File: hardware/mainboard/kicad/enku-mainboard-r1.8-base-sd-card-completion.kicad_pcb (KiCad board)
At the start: 4 copper layers, 59 x 101 mm, 132 parts, among them J1 1S LiPo + NTC, J2 Hirose DM3AT-SF-PEJM5, J3 FH34SRJ-24S-0.5SH(50), J5 GCT USB4105-GF-A-120, J6 4-pin pogo dock, J7 Tag-Connect TC2030-IDC-NL, Q1 IRLML6346TRPBF, Q2 AO3401A, SW1 HARD POWER, SW2 BOOT / RECOVERY, SW3 BTN_L1, SW4 BTN_L2, SW5 BTN_R1, SW6 BTN_R2, U1 ESP32-S3-WROOM-1-N16R8, U10 TLV3012BIDBVR, U2 TPS2121, U3 BQ25185DLHR, U4 TPS63802DLAR, U5 BMI270, U8 USBLC6-2SC6, U9 TMUX1101DBVR

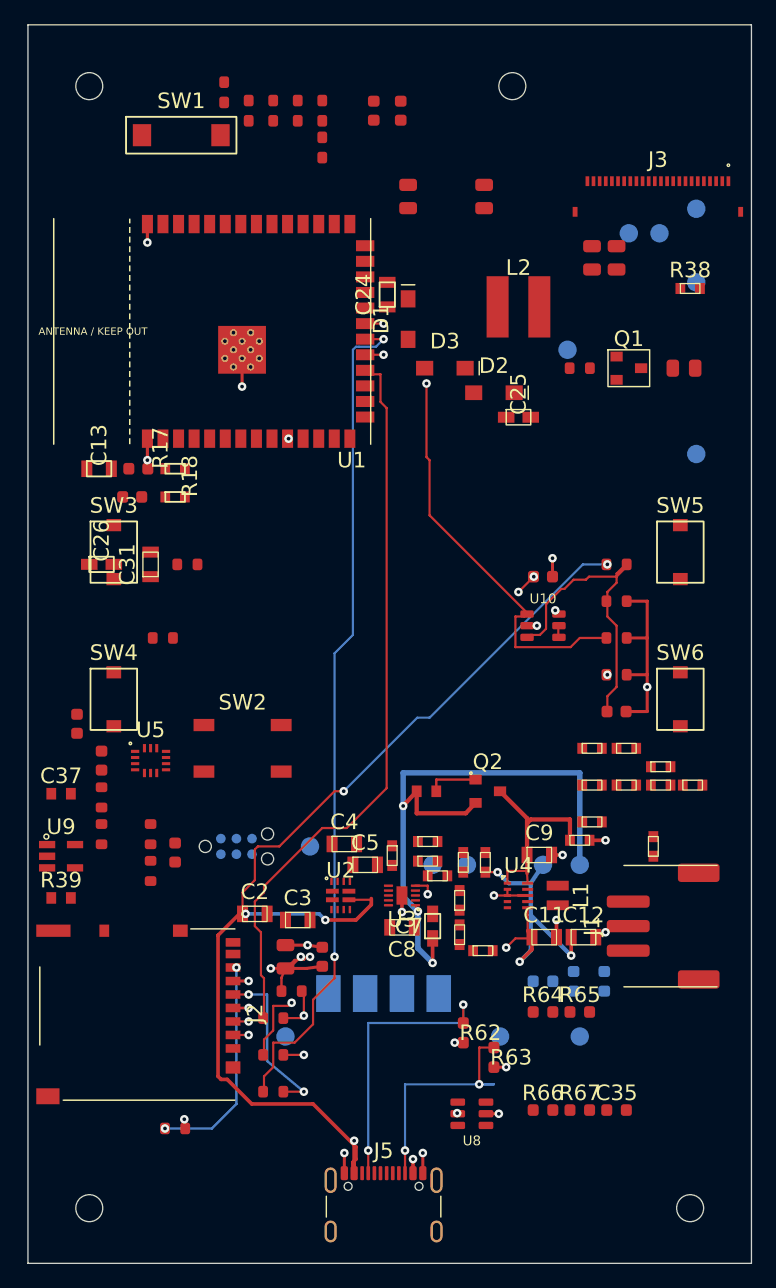
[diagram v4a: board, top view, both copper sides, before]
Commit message: R41: move new plated via holes out of SD, comparator and USB SMD lands
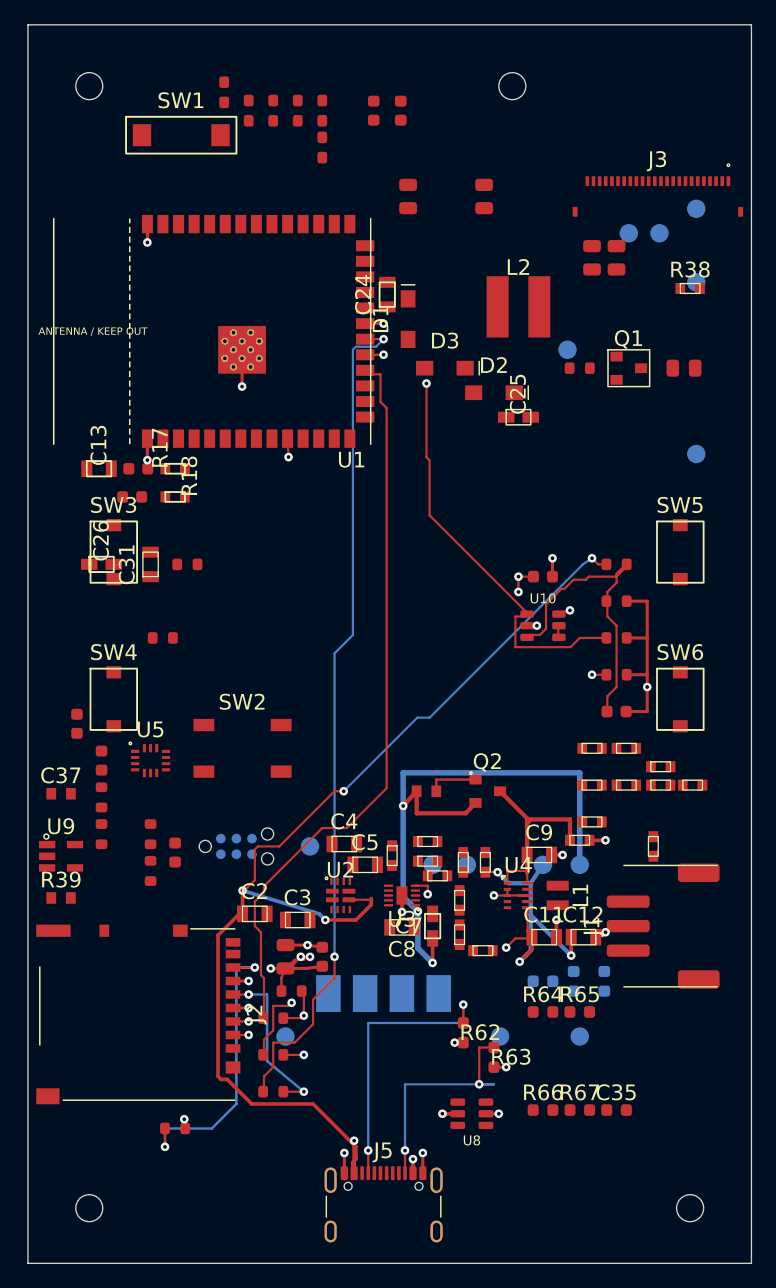
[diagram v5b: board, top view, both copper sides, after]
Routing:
- net VBUS_USB: track 134.1 -> 140.3 mm
- net SD_MISO_CARD: track 18.1 -> 24.1 mm
- net USB_VBUS_VALID: track 54.8 -> 57.8 mm
- net 3V3_SYS: track 101.8 -> 104.7 mm
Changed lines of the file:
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@@
   (segment (start 40.5 100.8) (end 40.3 101) (width 0.18) (layer "F.Cu") (net 9))
   (segment (start 40.3 101) (end 38.825 101) (width 0.18) (layer "F.Cu") (net 9))
-  (segment (start 34.725 96.875) (end 35 96.875) (width 0.18) (layer "F.Cu") (net 12))
+  (segment (start 34.725 96.875) (end 36.5 96.875) (width 0.18) (layer "F.Cu") (net 12))
   (segment (start 35 96.875) (end 35 108) (width 0.2) (layer "B.Cu") (net 12))
   (segment (start 35 108) (end 33 110) (width 0.2) (layer "B.Cu") (net 12))
@@
   (via (at 36 102.375) (size 0.70) (drill 0.30) (layers "F.Cu" "B.Cu") (net 9))
   (via (at 40.5 100.8) (size 0.70) (drill 0.30) (layers "F.Cu" "B.Cu") (net 9))
-  (via (at 35 96.875) (size 0.70) (drill 0.30) (layers "F.Cu" "B.Cu") (net 12))
-  (via (at 29.175 110) (size 0.70) (drill 0.30) (layers "F.Cu" "B.Cu") (net 12))
+  (via (at 36.5 96.875) (size 0.70) (drill 0.30) (layers "F.Cu" "B.Cu") (net 12))
+  (via (at 29.175 111.5) (size 0.70) (drill 0.30) (layers "F.Cu" "B.Cu") (net 12))
   (segment (start 45.5 48.25) (end 45.75 48.5) (width 0.18) (layer "F.Cu") (net 60))
   (segment (start 45.75 48.5) (end 46.75 48.5) (width 0.18) (layer "F.Cu") (net 60))
@@
   (segment (start 47.5 43.5) (end 46.5 43.5) (width 0.18) (layer "In1.Cu") (net 97))
   (segment (start 46.5 43.5) (end 39.25 50.75) (width 0.18) (layer "In1.Cu") (net 97))
-  (segment (start 39.25 50.75) (end 39.25 53.75) (width 0.18) (layer "In1.Cu") (net 97))
+  (segment (start 39.25 50.75) (end 39.25 55.25) (width 0.18) (layer "In1.Cu") (net 97))
   (via (at 50.5 49.25) (size 0.70) (drill 0.30) (layers "F.Cu" "B.Cu") (net 97))
-  (via (at 39.25 53.75) (size 0.70) (drill 0.30) (layers "F.Cu" "B.Cu") (net 97))
-  (segment (start 61.25 68.0) (end 61.0 67.75) (width 0.18) (layer "F.Cu") (net 2))
-  (segment (start 61.0 67.75) (end 59.25 66.0) (width 0.18) (layer "In1.Cu") (net 2))
-  (segment (start 59.25 66.0) (end 59.25 65.0) (width 0.18) (layer "In1.Cu") (net 2))
-  (via (at 61.0 67.75) (size 0.70) (drill 0.30) (layers "F.Cu" "B.Cu") (net 2))
-  (via (at 59.25 65.0) (size 0.70) (drill 0.30) (layers "F.Cu" "B.Cu") (net 2))
-  (segment (start 59.25 65.0) (end 58.0 66.25) (width 0.18) (layer "F.Cu") (net 2))
+  (via (at 39.25 55.25) (size 0.70) (drill 0.30) (layers "F.Cu" "B.Cu") (net 97))
+  (segment (start 61.25 68.0) (end 62.2 67.75) (width 0.18) (layer "F.Cu") (net 2))
+  (segment (start 62.2 67.75) (end 59.25 66.0) (width 0.18) (layer "In1.Cu") (net 2))
+  (segment (start 59.25 66.0) (end 58 65) (width 0.18) (layer "In1.Cu") (net 2))
+  (via (at 62.2 67.75) (size 0.70) (drill 0.30) (layers "F.Cu" "B.Cu") (net 2))
+  (via (at 58 65) (size 0.70) (drill 0.30) (layers "F.Cu" "B.Cu") (net 2))
+  (segment (start 58 65) (end 58.0 66.25) (width 0.18) (layer "F.Cu") (net 2))
   (segment (start 58.0 66.25) (end 49.5 74.75) (width 0.18) (layer "In1.Cu") (net 2))
   (segment (start 49.5 74.75) (end 49.5 84.25) (width 0.18) (layer "In1.Cu") (net 2))
@@
   (segment (start 49.75 76.5) (end 50.75 76.5) (width 0.18) (layer "B.Cu") (net 3))
   (segment (start 50.75 76.5) (end 63.25 64.0) (width 0.18) (layer "B.Cu") (net 3))
-  (segment (start 63.25 64.0) (end 65.25 64.0) (width 0.18) (layer "B.Cu") (net 3))
+  (segment (start 63.25 64.0) (end 64 63.5) (width 0.18) (layer "B.Cu") (net 3))
   (via (at 43.75 82.5) (size 0.70) (drill 0.30) (layers "F.Cu" "B.Cu") (net 3))
-  (via (at 65.25 64.0) (size 0.70) (drill 0.30) (layers "F.Cu" "B.Cu") (net 3))
-  (segment (start 65.25 64.0) (end 65.25 73.0) (width 0.18) (layer "In1.Cu") (net 3))
-  (via (at 65.25 73.0) (size 0.70) (drill 0.30) (layers "F.Cu" "B.Cu") (net 3))
+  (via (at 64 63.5) (size 0.70) (drill 0.30) (layers "F.Cu" "B.Cu") (net 3))
+  (segment (start 64 63.5) (end 64 73) (width 0.18) (layer "In1.Cu") (net 3))
+  (via (at 64 73) (size 0.70) (drill 0.30) (layers "F.Cu" "B.Cu") (net 3))
   (zone (net 1) (net_name "GND") (layer "In1.Cu") (hatch edge 0.5)
     (connect_pads (clearance 0.25))
@@
   (segment (start 33.5 94.25) (end 35.25 92.5) (width 0.30) (layer "F.Cu") (net 3))
   (segment (start 35.25 92.5) (end 35.5 92.5) (width 0.30) (layer "F.Cu") (net 3))
-  (segment (start 35.5 92.5) (end 35.75 92.5) (width 0.30) (layer "F.Cu") (net 3))
-  (segment (start 35.75 92.5) (end 41.75 92.5) (width 0.30) (layer "B.Cu") (net 3))
+  (segment (start 35.5 92.5) (end 35.5 90.6) (width 0.30) (layer "F.Cu") (net 3))
+  (segment (start 35.5 90.6) (end 41.75 92.5) (width 0.30) (layer "B.Cu") (net 3))
   (segment (start 41.75 92.5) (end 42.25 93.0) (width 0.30) (layer "B.Cu") (net 3))
   (segment (start 42.25 93.0) (end 44.75 93.0) (width 0.30) (layer "F.Cu") (net 3))
   (segment (start 44.75 93.0) (end 46.0 91.75) (width 0.30) (layer "F.Cu") (net 3))
   (segment (start 46.0 91.75) (end 46.0 91.25) (width 0.30) (layer "F.Cu") (net 3))
-  (via (at 35.75 92.5) (size 0.70) (drill 0.30) (layers "F.Cu" "B.Cu") (net 3))
+  (via (at 35.5 90.6) (size 0.70) (drill 0.30) (layers "F.Cu" "B.Cu") (net 3))
   (via (at 42.25 93.0) (size 0.70) (drill 0.30) (layers "F.Cu" "B.Cu") (net 3))
-  (segment (start 35.5 92.5) (end 35.75 92.5) (width 0.30) (layer "F.Cu") (net 3))
-  (segment (start 35.75 92.5) (end 38.75 95.75) (width 0.30) (layer "In1.Cu") (net 3))
+  (segment (start 35.5 90.6) (end 38.75 95.75) (width 0.30) (layer "In1.Cu") (net 3))
   (segment (start 38.75 95.75) (end 38.75 100.5) (width 0.30) (layer "In1.Cu") (net 3))
   (segment (start 38.75 100.5) (end 45.25 107.0) (width 0.30) (layer "In1.Cu") (net 3))
   (segment (start 45.25 107.0) (end 51.25 107.0) (width 0.30) (layer "In1.Cu") (net 3))
-  (segment (start 51.25 107.0) (end 53.0 108.75) (width 0.30) (layer "In1.Cu") (net 3))
-  (via (at 53.0 108.75) (size 0.70) (drill 0.30) (layers "F.Cu" "B.Cu") (net 3))
+  (segment (start 51.25 107.0) (end 51.8 108.8) (width 0.30) (layer "In1.Cu") (net 3))
+  (via (at 51.8 108.8) (size 0.70) (drill 0.30) (layers "F.Cu" "B.Cu") (net 3))
   (segment (start 54.8 103.4) (end 56 103.4) (width 0.18) (layer "F.Cu") (net 5))
-)
+  (segment (start 36.5 96.875) (end 35 96.875) (width .2) (layer "B.Cu") (net 12))
+  (segment (start 29.175 110) (end 29.175 111.5) (width .2) (layer "B.Cu") (net 12))
+  (segment (start 29.175 110) (end 29.175 111.5) (width .18) (layer "F.Cu") (net 12))
+  (segment (start 39.175 53.75) (end 39.25 55.25) (width .18) (layer "F.Cu") (net 97))
+  (segment (start 58 65) (end 59.225 65) (width .18) (layer "F.Cu") (net 2))
+  (segment (start 64 63.5) (end 64.5 64) (width .18) (layer "F.Cu") (net 3))
+  (segment (start 64.5 64) (end 65.175 64) (width .18) (layer "F.Cu") (net 3))
+  (segment (start 64 73) (end 65.175 73) (width .18) (layer "F.Cu") (net 3))
+  (segment (start 51.8 108.8) (end 53.05 108.8) (width .3) (layer "F.Cu") (net 3))
+)

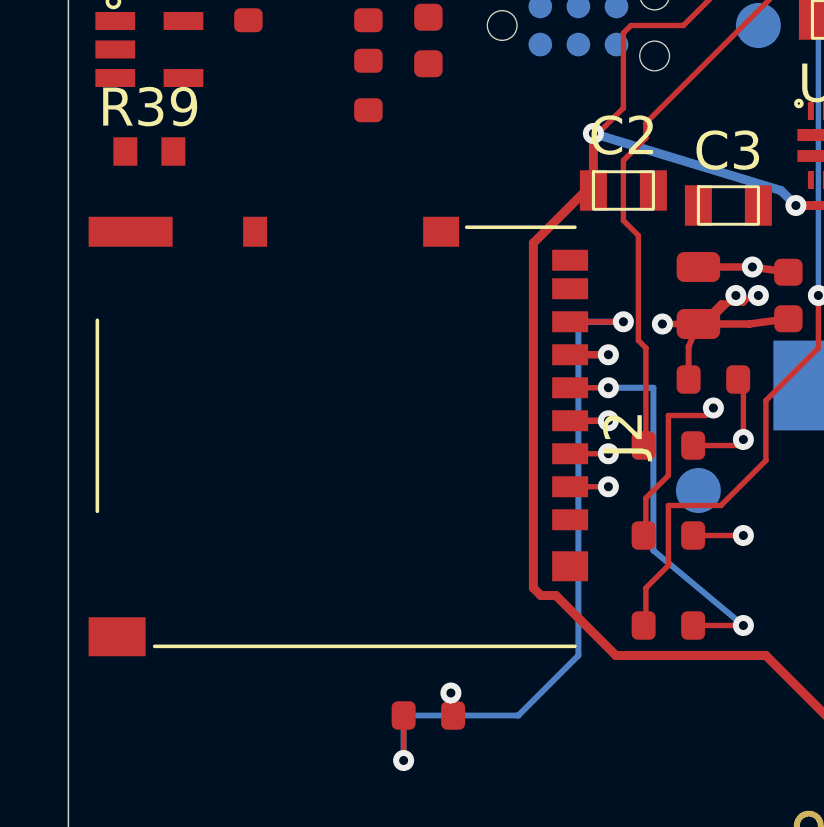
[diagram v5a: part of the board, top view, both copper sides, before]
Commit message: R41: complete all microSD ground contacts and native functional continuity gate
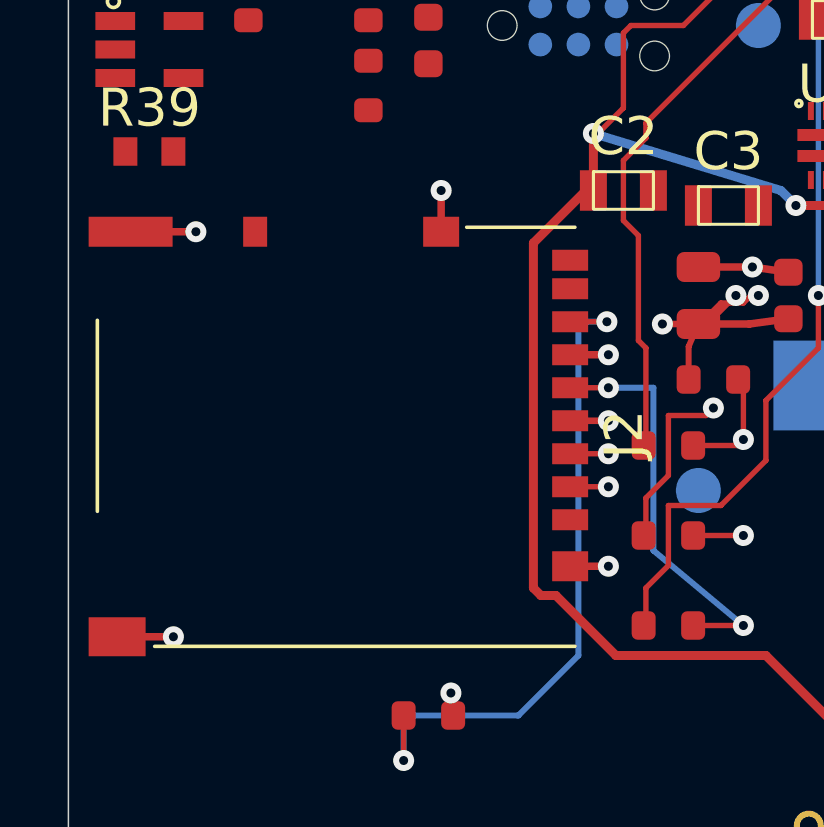
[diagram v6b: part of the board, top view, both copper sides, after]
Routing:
- net GND: track 45.2 -> 51.9 mm, vias 20 -> 24
- net SD_MISO_CARD: track 24.1 -> 23.0 mm
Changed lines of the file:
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@@
     (min_thickness 0.25)
     (fill yes (thermal_gap 0.30) (thermal_bridge_width 0.30))
-    (polygon (pts (xy 27 35) (xy 69 35) (xy 69 119) (xy 27 119)))
+    (polygon (pts (xy 27 35) (xy 69 35) (xy 69 80) (xy 75 80) (xy 75 119) (xy 18.5 119) (xy 18.5 80) (xy 27 80)))
   )
   (segment (start 39 95.05) (end 40.8 95.05) (width 0.25) (layer "F.Cu") (net 1))
@@
   (segment (start 40.5 100.8) (end 40.3 101) (width 0.18) (layer "F.Cu") (net 9))
   (segment (start 40.3 101) (end 38.825 101) (width 0.18) (layer "F.Cu") (net 9))
-  (segment (start 34.725 96.875) (end 36.5 96.875) (width 0.18) (layer "F.Cu") (net 12))
+  (segment (start 34.725 96.875) (end 35.95 96.875) (width 0.18) (layer "F.Cu") (net 12))
   (segment (start 35 96.875) (end 35 108) (width 0.2) (layer "B.Cu") (net 12))
   (segment (start 35 108) (end 33 110) (width 0.2) (layer "B.Cu") (net 12))
@@
   (via (at 36 102.375) (size 0.70) (drill 0.30) (layers "F.Cu" "B.Cu") (net 9))
   (via (at 40.5 100.8) (size 0.70) (drill 0.30) (layers "F.Cu" "B.Cu") (net 9))
-  (via (at 36.5 96.875) (size 0.70) (drill 0.30) (layers "F.Cu" "B.Cu") (net 12))
+  (via (at 35.95 96.875) (size 0.70) (drill 0.30) (layers "F.Cu" "B.Cu") (net 12))
   (via (at 29.175 111.5) (size 0.70) (drill 0.30) (layers "F.Cu" "B.Cu") (net 12))
   (segment (start 45.5 48.25) (end 45.75 48.5) (width 0.18) (layer "F.Cu") (net 60))
@@
     (min_thickness 0.25)
     (fill yes (thermal_gap 0.30) (thermal_bridge_width 0.30))
-    (polygon (pts (xy 27 35) (xy 69 35) (xy 69 119) (xy 27 119)))
+    (polygon (pts (xy 27 35) (xy 69 35) (xy 69 80) (xy 75 80) (xy 75 119) (xy 18.5 119) (xy 18.5 80) (xy 27 80)))
   )
   (segment (start 27.74 53.75) (end 27.74 55.5) (width 0.25) (layer "F.Cu") (net 1))
@@
   (via (at 51.8 108.8) (size 0.70) (drill 0.30) (layers "F.Cu" "B.Cu") (net 3))
   (segment (start 54.8 103.4) (end 56 103.4) (width 0.18) (layer "F.Cu") (net 5))
-  (segment (start 36.5 96.875) (end 35 96.875) (width .2) (layer "B.Cu") (net 12))
+  (segment (start 35.95 96.875) (end 35 96.875) (width .2) (layer "B.Cu") (net 12))
   (segment (start 29.175 110) (end 29.175 111.5) (width .2) (layer "B.Cu") (net 12))
   (segment (start 29.175 110) (end 29.175 111.5) (width .18) (layer "F.Cu") (net 12))
@@
   (segment (start 64 73) (end 65.175 73) (width .18) (layer "F.Cu") (net 3))
   (segment (start 51.8 108.8) (end 53.05 108.8) (width .3) (layer "F.Cu") (net 3))
-)
+  (segment (start 34.725 105.025) (end 36 105.025) (width 0.25) (layer "F.Cu") (net 1))
+  (via (at 36 105.025) (size 0.70) (drill 0.30) (layers "F.Cu" "B.Cu") (net 1))
+  (segment (start 30.425 93.875) (end 30.425 92.5) (width 0.25) (layer "F.Cu") (net 1))
+  (via (at 30.425 92.5) (size 0.70) (drill 0.30) (layers "F.Cu" "B.Cu") (net 1))
+  (segment (start 20.075 93.875) (end 22.25 93.875) (width 0.25) (layer "F.Cu") (net 1))
+  (via (at 22.25 93.875) (size 0.70) (drill 0.30) (layers "F.Cu" "B.Cu") (net 1))
+  (segment (start 19.625 107.375) (end 21.5 107.375) (width 0.25) (layer "F.Cu") (net 1))
+  (via (at 21.5 107.375) (size 0.70) (drill 0.30) (layers "F.Cu" "B.Cu") (net 1))
+)

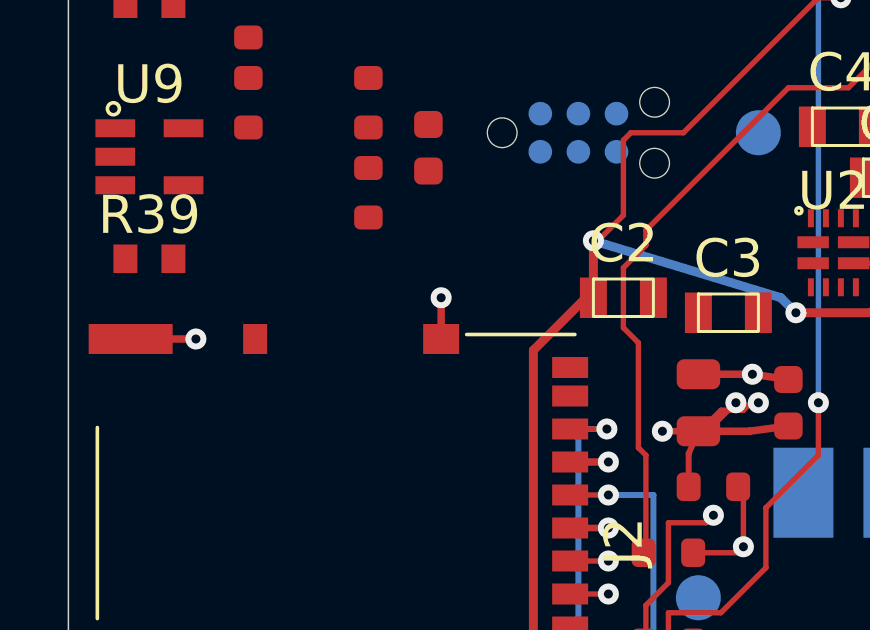
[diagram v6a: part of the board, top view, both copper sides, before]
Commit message: R41: clear card shell return from MISO and register every active-board part
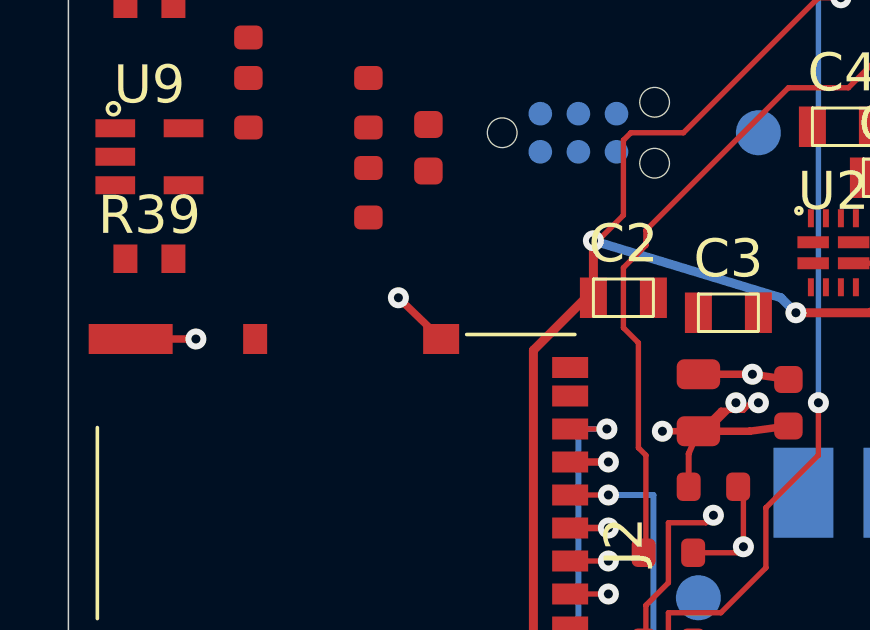
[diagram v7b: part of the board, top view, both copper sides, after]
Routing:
- net GND: track 51.9 -> 52.5 mm
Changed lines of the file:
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@@
   (segment (start 34.725 105.025) (end 36 105.025) (width 0.25) (layer "F.Cu") (net 1))
   (via (at 36 105.025) (size 0.70) (drill 0.30) (layers "F.Cu" "B.Cu") (net 1))
-  (segment (start 30.425 93.875) (end 30.425 92.5) (width 0.25) (layer "F.Cu") (net 1))
-  (via (at 30.425 92.5) (size 0.70) (drill 0.30) (layers "F.Cu" "B.Cu") (net 1))
+  (segment (start 30.425 93.875) (end 29 92.5) (width 0.25) (layer "F.Cu") (net 1))
+  (via (at 29 92.5) (size 0.70) (drill 0.30) (layers "F.Cu" "B.Cu") (net 1))
   (segment (start 20.075 93.875) (end 22.25 93.875) (width 0.25) (layer "F.Cu") (net 1))
   (via (at 22.25 93.875) (size 0.70) (drill 0.30) (layers "F.Cu" "B.Cu") (net 1))
